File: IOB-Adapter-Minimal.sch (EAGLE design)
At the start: 1 part

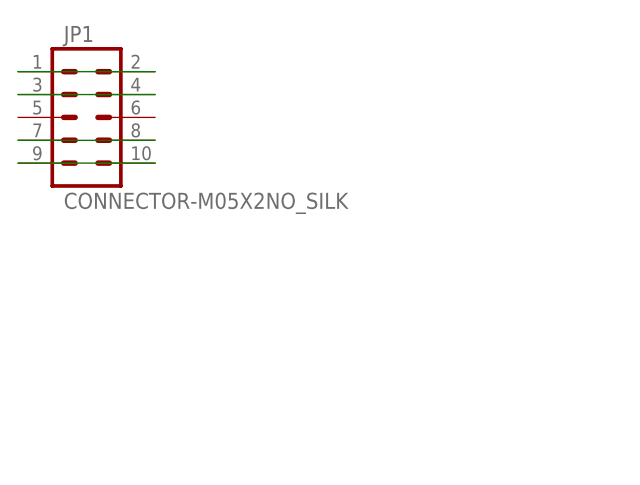
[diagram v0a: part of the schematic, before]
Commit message: normalized values
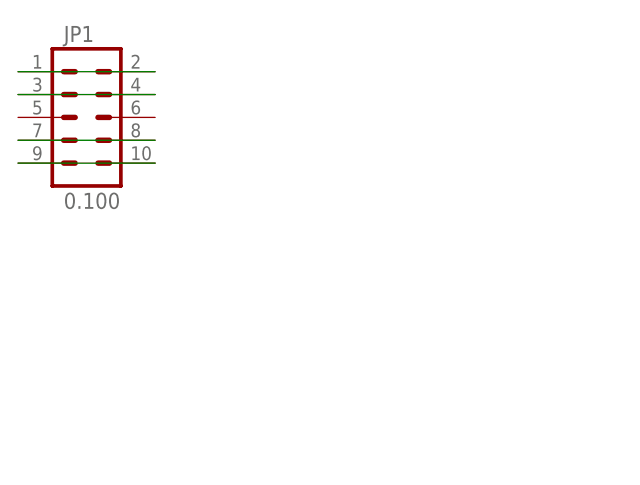
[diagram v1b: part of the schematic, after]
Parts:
- JP1: value CONNECTOR-M05X2NO_SILK -> 0.100
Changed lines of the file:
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@@
 <grid distance="100" unitdist="mil" unit="mil" style="dots" multiple="1" display="yes" altdistance="50" altunitdist="mil" altunit="mil"/>
 <layers>
-<layer number="1" name="Top" color="4" fill="1" visible="yes" active="no"/>
-<layer number="2" name="Route2" color="1" fill="3" visible="yes" active="no"/>
-<layer number="3" name="Route3" color="4" fill="3" visible="yes" active="no"/>
-<layer number="14" name="Route14" color="1" fill="6" visible="yes" active="no"/>
-<layer number="15" name="Route15" color="4" fill="6" visible="yes" active="no"/>
-<layer number="16" name="Bottom" color="2" fill="1" visible="yes" active="no"/>
-<layer number="17" name="Pads" color="23" fill="1" visible="yes" active="no"/>
-<layer number="18" name="Vias" color="29" fill="1" visible="yes" active="no"/>
-<layer number="19" name="Unrouted" color="6" fill="1" visible="yes" active="no"/>
-<layer number="20" name="Dimension" color="15" fill="1" visible="yes" active="no"/>
-<layer number="21" name="tPlace" color="19" fill="1" visible="yes" active="no"/>
-<layer number="22" name="bPlace" color="17" fill="1" visible="yes" active="no"/>
-<layer number="23" name="tOrigins" color="30" fill="1" visible="yes" active="no"/>
-<layer number="24" name="bOrigins" color="15" fill="1" visible="yes" active="no"/>
-<layer number="25" name="tNames" color="63" fill="1" visible="yes" active="no"/>
-<layer number="26" name="bNames" color="34" fill="1" visible="yes" active="no"/>
-<layer number="27" name="tValues" color="56" fill="1" visible="yes" active="no"/>
-<layer number="28" name="bValues" color="7" fill="1" visible="yes" active="no"/>
+<layer number="1" name="Top" color="4" fill="1" visible="no" active="no"/>
+<layer number="2" name="Route2" color="1" fill="3" visible="no" active="no"/>
+<layer number="3" name="Route3" color="4" fill="3" visible="no" active="no"/>
+<layer number="14" name="Route14" color="1" fill="6" visible="no" active="no"/>
+<layer number="15" name="Route15" color="4" fill="6" visible="no" active="no"/>
+<layer number="16" name="Bottom" color="2" fill="1" visible="no" active="no"/>
+<layer number="17" name="Pads" color="23" fill="1" visible="no" active="no"/>
+<layer number="18" name="Vias" color="29" fill="1" visible="no" active="no"/>
+<layer number="19" name="Unrouted" color="6" fill="1" visible="no" active="no"/>
+<layer number="20" name="Dimension" color="15" fill="1" visible="no" active="no"/>
+<layer number="21" name="tPlace" color="19" fill="1" visible="no" active="no"/>
+<layer number="22" name="bPlace" color="17" fill="1" visible="no" active="no"/>
+<layer number="23" name="tOrigins" color="30" fill="1" visible="no" active="no"/>
+<layer number="24" name="bOrigins" color="15" fill="1" visible="no" active="no"/>
+<layer number="25" name="tNames" color="63" fill="1" visible="no" active="no"/>
+<layer number="26" name="bNames" color="34" fill="1" visible="no" active="no"/>
+<layer number="27" name="tValues" color="56" fill="1" visible="no" active="no"/>
+<layer number="28" name="bValues" color="7" fill="1" visible="no" active="no"/>
 <layer number="29" name="tStop" color="7" fill="3" visible="no" active="no"/>
 <layer number="30" name="bStop" color="7" fill="6" visible="no" active="no"/>
@@
 <layer number="35" name="tGlue" color="7" fill="4" visible="no" active="no"/>
 <layer number="36" name="bGlue" color="7" fill="5" visible="no" active="no"/>
-<layer number="37" name="tTest" color="7" fill="1" visible="yes" active="no"/>
-<layer number="38" name="bTest" color="7" fill="1" visible="yes" active="no"/>
+<layer number="37" name="tTest" color="7" fill="1" visible="no" active="no"/>
+<layer number="38" name="bTest" color="7" fill="1" visible="no" active="no"/>
 <layer number="39" name="tKeepout" color="4" fill="11" visible="no" active="no"/>
 <layer number="40" name="bKeepout" color="3" fill="11" visible="no" active="no"/>
@@
 <layer number="44" name="Drills" color="16" fill="1" visible="no" active="no"/>
 <layer number="45" name="Holes" color="35" fill="1" visible="no" active="no"/>
-<layer number="46" name="Milling" color="35" fill="1" visible="yes" active="no"/>
-<layer number="47" name="Measures" color="21" fill="1" visible="yes" active="no"/>
-<layer number="48" name="Document" color="36" fill="1" visible="yes" active="no"/>
-<layer number="49" name="Reference" color="48" fill="1" visible="yes" active="no"/>
-<layer number="50" name="dxf" color="7" fill="1" visible="yes" active="no"/>
-<layer number="51" name="tDocu" color="24" fill="1" visible="yes" active="no"/>
-<layer number="52" name="bDocu" color="7" fill="1" visible="yes" active="no"/>
-<layer number="53" name="tGND_GNDA" color="7" fill="9" visible="yes" active="no"/>
-<layer number="54" name="bGND_GNDA" color="1" fill="9" visible="yes" active="no"/>
-<layer number="56" name="wert" color="7" fill="1" visible="yes" active="no"/>
-<layer number="57" name="tCAD" color="7" fill="1" visible="yes" active="no"/>
-<layer number="59" name="tCarbon" color="7" fill="1" visible="yes" active="no"/>
-<layer number="60" name="bCarbon" color="7" fill="1" visible="yes" active="no"/>
+<layer number="46" name="Milling" color="35" fill="1" visible="no" active="no"/>
+<layer number="47" name="Measures" color="21" fill="1" visible="no" active="no"/>
+<layer number="48" name="Document" color="36" fill="1" visible="no" active="no"/>
+<layer number="49" name="Reference" color="48" fill="1" visible="no" active="no"/>
+<layer number="50" name="dxf" color="7" fill="1" visible="no" active="no"/>
+<layer number="51" name="tDocu" color="24" fill="1" visible="no" active="no"/>
+<layer number="52" name="bDocu" color="7" fill="1" visible="no" active="no"/>
+<layer number="53" name="tGND_GNDA" color="7" fill="9" visible="no" active="no"/>
+<layer number="54" name="bGND_GNDA" color="1" fill="9" visible="no" active="no"/>
+<layer number="56" name="wert" color="7" fill="1" visible="no" active="no"/>
+<layer number="57" name="tCAD" color="7" fill="1" visible="no" active="no"/>
+<layer number="59" name="tCarbon" color="7" fill="1" visible="no" active="no"/>
+<layer number="60" name="bCarbon" color="7" fill="1" visible="no" active="no"/>
 <layer number="90" name="Modules" color="5" fill="1" visible="yes" active="yes"/>
 <layer number="91" name="Nets" color="2" fill="1" visible="yes" active="yes"/>
@@
 <parts>
 <part name="FRAME2" library="SPCoast" deviceset="DOC-FRAME-LETTER" device=""/>
-<part name="JP1" library="SPCoast" deviceset="CONNECTOR-M05X2" device="NO_SILK" value="CONNECTOR-M05X2NO_SILK"/>
+<part name="JP1" library="SPCoast" deviceset="CONNECTOR-M05X2" device="NO_SILK" value="0.100"/>
 </parts>
 <sheets>
